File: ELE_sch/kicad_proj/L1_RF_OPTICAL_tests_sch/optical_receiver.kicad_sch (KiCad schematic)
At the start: 2 parts, among them U1 MCP601-xP

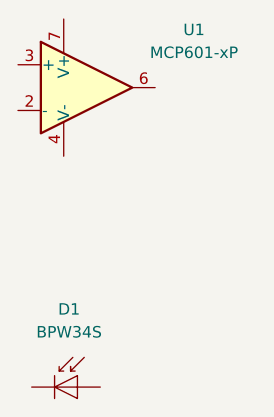
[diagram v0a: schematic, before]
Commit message: update microcontrollers settings, taksks list, RF and LED cricuiits
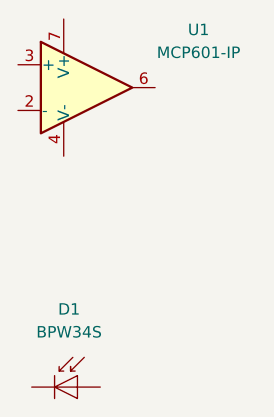
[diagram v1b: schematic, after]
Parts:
- U1: value MCP601-xP -> MCP601-IP
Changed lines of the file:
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@@
 		(fields_autoplaced yes)
 		(property "Reference" "U1"
-			(at 159.512 84.2578 0)
+			(at 160.02 84.2578 0)
 			(show_name no)
 			(do_not_autoplace no)
@@
 			)
 		)
-		(property "Value" "MCP601-xP"
-			(at 159.512 86.7978 0)
+		(property "Value" "MCP601-IP"
+			(at 160.02 86.7978 0)
 			(show_name no)
 			(do_not_autoplace no)
